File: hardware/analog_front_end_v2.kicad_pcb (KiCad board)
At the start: 4 copper layers, 142.9 x 41.4 mm, 101 parts, among them J1 Conn_Coaxial, J3 Conn_01x01_Socket, J4 Conn_01x01_Socket, U1 ADL5531, U10 MAX6002, U11 LP2985-5.0, U12 MAX2606, U13 PAT1220-C-0DB, U14 LP2985-5.0, U15 BFP540ESD, U16 BFP540ESD, U17 LP2985-3.3, U18 PAT1220-C-0DB, U19 PAT1220-C-0DB, U2 ADL5531, U20 PAT1220-C-0DB, U21 PAT1220-C-0DB, U3 ADL5531, U4 ADL5531, U5 LP2985-1.8, U6 MCP33131, U7 PAT1220-C-0DB, U8 ADL5531, U9 PMOD 2x6

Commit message: Latest KiCAD9.0 project file
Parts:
- renumbered TP22 to GND
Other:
- board size 142.9 x 41.4 mm -> 145 x 44 mm
- board text added: "Decisions: Dimensions: 145mm x 44mm Use Coplanar Waveguide for RF filter section for more confined EM fields Use 0.6x0.3 vias Use 7mil trace for CPW section with 4mil gap to coplanar ground (Standard PCB manufacturer limit) assuming 1ounce copper, 0.1mm high prepreg, 4.6 dielectric constant Use 1mm via distance (2xgap) Use 2mm between vias horizontally Use 7mil for microstrip for around 50ohm imp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"
- board text removed: "TODO: Add solid GND planes on layers 2/3 Ground via stitching Decisions: Use Coplanar Waveguide for RF filter section for more confined EM fields Use 0.6x0.3 vias Use 8mil trace with 0.05mm airgap assuming 1ounce copper, 4.6 dielectric constant Use 1mm via distance (2xgap) Use 2mm between vias horizontally for microstrip with solid groundplane in layers 2,3 oriented horizontally for EM fields Use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"

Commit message: Updated KiCAD prj/sch/pcb files that were sent for manufacturing
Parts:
- U6: footprint Package_SO:MSOP-10_3x3mm_P0.5mm -> TheEEView_Footprint_Lib:MCP33131
- renumbered GND to TP22
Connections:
- net ADC_VREF renamed ADC_VREF_2V5

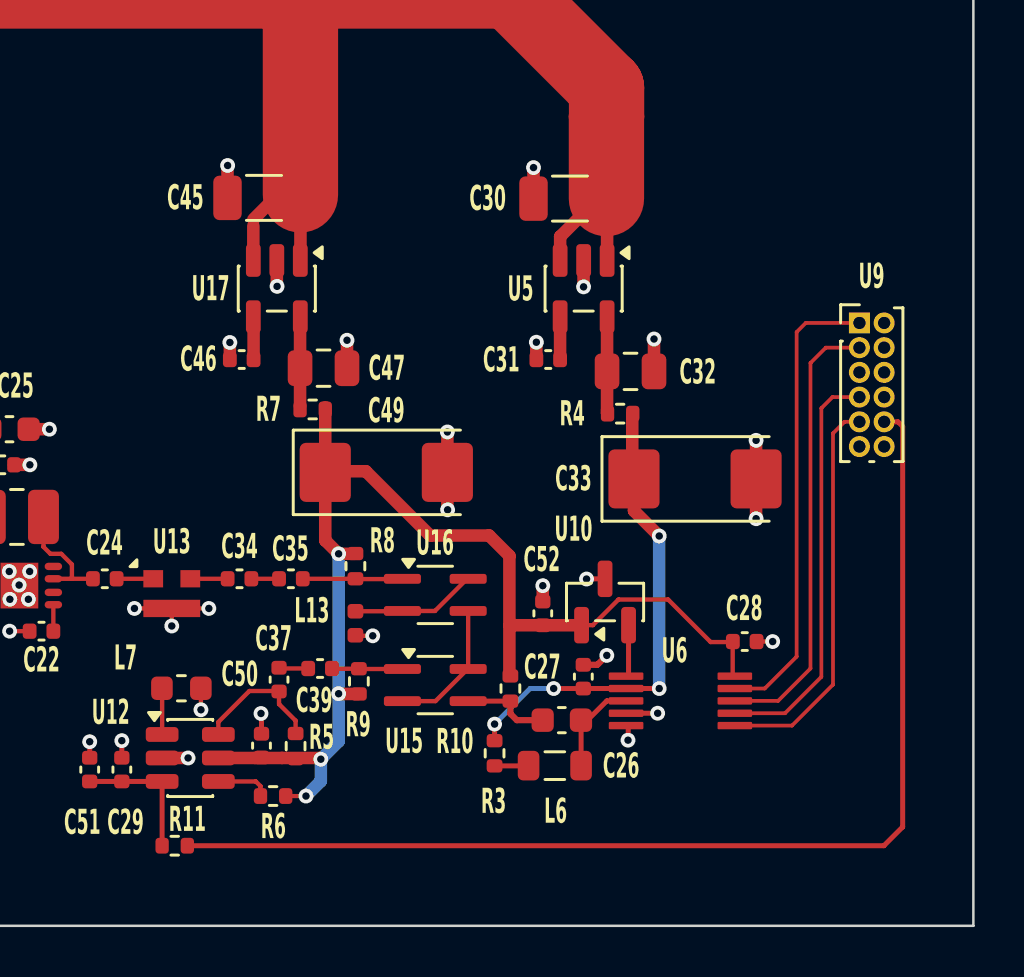
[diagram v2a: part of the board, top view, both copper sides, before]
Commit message: Updated KiCAD Prj,sch,pcb files for 2.54mm PMOD male connector
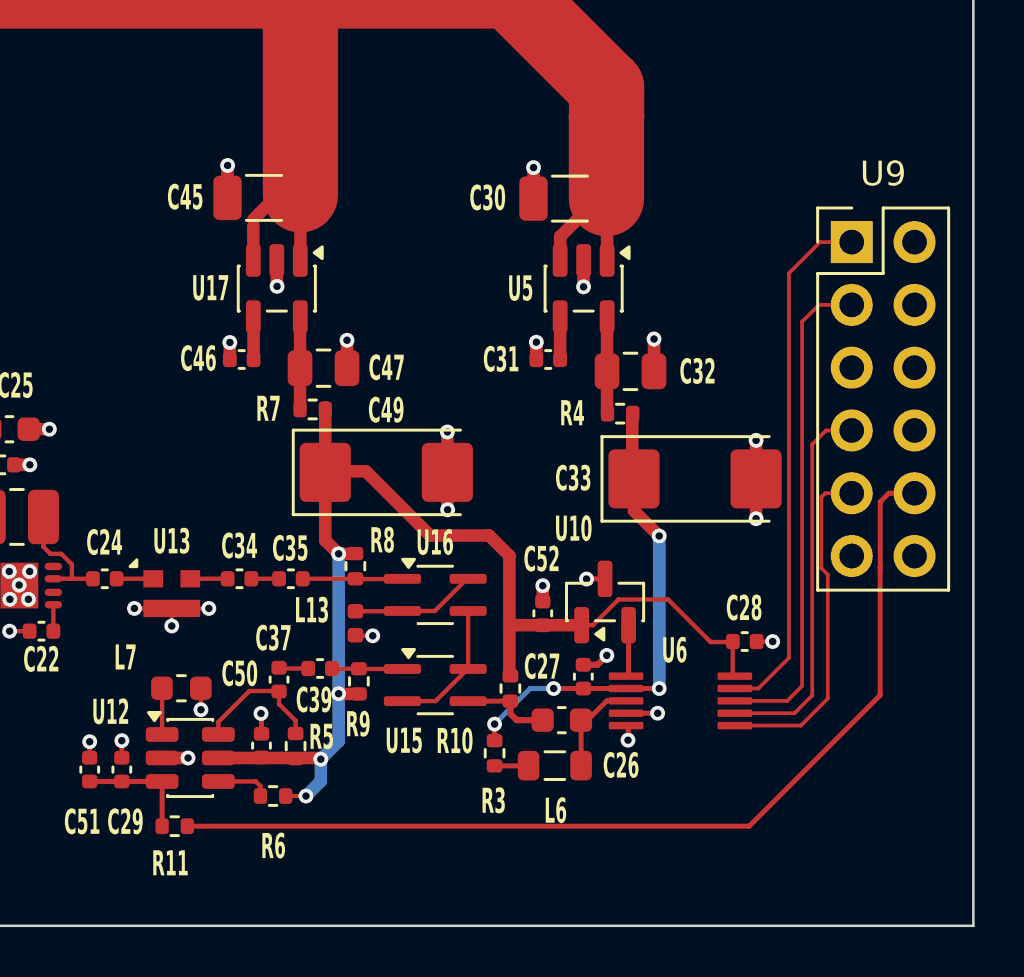
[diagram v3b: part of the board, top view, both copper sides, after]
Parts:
- U9: footprint Connector_PinHeader_1.00mm:PinHeader_2x06_P1.00mm_Vertical -> Connector_PinHeader_2.54mm:PinHeader_2x06_P2.54mm_Vertical
- moved U9 3.28 mm to (152.1, 26.9)
- moved R11 0.79 mm to (124.7, 50.6)
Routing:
- net PWM_TUNE: track 46.3 -> 39.6 mm
- net ADC_SDI: track 18.9 -> 21.4 mm
- net ADC_CONVST: track 16.2 -> 13.9 mm
- net ADC_SCLK: track 18.2 -> 20.0 mm
- net ADC_SDO: track 16.7 -> 16.1 mm
- net Net-(U12-TUNE): track 5.32 -> 4.74 mm

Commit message: Update prj/sch/pcb files sent off for manufacturing
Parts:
- added C53: 10n_25V, Capacitor_SMD:C_0402_1005Metric, F.Cu at (142.3, 52.0)
- added C54: 100n_25V, Capacitor_SMD:C_0402_1005Metric, F.Cu at (140.0, 49.2)
- added R2: 100, Resistor_SMD:R_0402_1005Metric, F.Cu at (141.1, 52.0)
- added U22: MCP6286, Package_TO_SOT_SMD:SOT-23-5, F.Cu at (138.4, 51.6)
- U9: value PMOD 2x6 -> PMOD 2x6 2.54mm pitch
- moved C26 4.45 mm to (142.6, 50.1), turned to 180 degrees
- moved R3 2.82 mm to (140.0, 46.0), turned to 0 degrees
- moved TP22 1.16 mm to (103.1, 46.2)
- moved R11 0.84 mm to (124.7, 51.4)
- moved L6 0.50 mm to (140.3, 47.7)
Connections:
- C26 pad 1: Net-(U15-C) -> Net-(C26-Pad1)
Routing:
- net 3V3: track 48.4 -> 59.2 mm
- net Net-(U15-C): track 3.63 -> 11.5 mm
- net Net-(U22-Vin-): track 0.00 -> 4.96 mm
- net Net-(C26-Pad1): track 0.00 -> 3.26 mm
- net GND: track 81.1 -> 84.2 mm, vias 163 -> 167
- net PWM_TUNE: track 39.6 -> 41.9 mm
- net 1V8: track 18.8 -> 16.5 mm, vias 4 -> 2
- net Net-(U6-AIN+): track 4.10 -> 5.79 mm
- net Net-(L6-Pad2): track 1.38 -> 2.32 mm
- net Net-(U12-TUNE): track 4.74 -> 5.58 mm
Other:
- board size 145 x 44 mm -> 146.1 x 45.5 mm
- board text added: "Decisions: Dimensions: 146mm x 45.5mm Use Coplanar Waveguide for RF filter section for more confined EM fields Use 0.6x0.3 vias Use 7mil trace for CPW section with 4mil gap to coplanar ground (Standard PCB manufacturer limit) assuming 1ounce copper, 0.1mm high prepreg, 4.6 dielectric constant Use 1mm via distance (2xgap) Use 2mm between vias horizontally Use 7mil for microstrip for around 50ohm i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"
- board text removed: "Decisions: Dimensions: 145mm x 44mm Use Coplanar Waveguide for RF filter section for more confined EM fields Use 0.6x0.3 vias Use 7mil trace for CPW section with 4mil gap to coplanar ground (Standard PCB manufacturer limit) assuming 1ounce copper, 0.1mm high prepreg, 4.6 dielectric constant Use 1mm via distance (2xgap) Use 2mm between vias horizontally Use 7mil for microstrip for around 50ohm imp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"
